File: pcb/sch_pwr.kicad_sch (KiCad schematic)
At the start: 10 parts, among them J3 Conn_01x03_Pin, U3 AP2112K-3.3, U4 AMS1117-5.0

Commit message: feat(sch): schematic review
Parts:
- removed C12, C14: 1uF, PCM_JLCPCB:C_0603, symbol PCM_JLCPCB-Capacitors:0603,1uF
- removed C15: 22uF, Capacitor_THT:CP_Radial_D4.0mm_P2.00mm, symbol EasyEDA:RVT1H220M0605
- removed H1: Jumper_Shunt, symbol Auxiliary_Items:Jumper_Shunt
- removed J3: Conn_01x03_Pin, Connector_PinHeader_2.54mm:PinHeader_1x03_P2.54mm_Vertical, symbol Connector:Conn_01x03_Pin
- removed U3: AP2112K-3.3, Package_TO_SOT_SMD:SOT-23-5, symbol Regulator_Linear:AP2112K-3.3
- removed U4: AMS1117-5.0, Package_TO_SOT_SMD:SOT-223-3_TabPin2, symbol Regulator_Linear:AMS1117-5.0
- added C14: 100uF, Capacitor_THT:CP_Radial_D5.0mm_P2.00mm, symbol PCM_JLCPCB-Capacitors:CASE-A-3216-18(mm),10uF
- added C27: 10uF, Capacitor_THT:CP_Radial_D5.0mm_P2.00mm, symbol PCM_JLCPCB-Capacitors:CASE-A-3216-18(mm),10uF
- added C28: 4.7uF, Capacitor_THT:CP_Radial_D5.0mm_P2.00mm, symbol PCM_JLCPCB-Capacitors:CASE-A-3216-18(mm),10uF
- added D3: D, Diode_SMD:D_SMA, symbol Device:D
- added D9: PLZ3V3B, Diode_SMD:D_SMF, symbol Device:D_Schottky
- added F1, F2: Polyfuse, Fuse:Fuse_1206_3216Metric, symbol Device:Polyfuse
- added SW2: SW_Lever_RSPRO_5MS1, library:SW_Lever_RSPRO_5MS1, symbol library:SW_Lever_RSPRO_5MS1
- added U2: LD1117S33TR_SOT223, Package_TO_SOT_SMD:SOT-223-3_TabPin2, symbol Regulator_Linear:LD1117S33TR_SOT223
- added U3: LD1117S50TR_SOT223, Package_TO_SOT_SMD:SOT-223-3_TabPin2, symbol Regulator_Linear:LD1117S50TR_SOT223
- C13: value 10uF -> 1uF; footprint PCM_JLCPCB:C_CASE-A-3216-18(mm) -> Capacitor_THT:CP_Radial_D5.0mm_P2.00mm; Rated Voltage 16V -> 25V
- D8: value D_Schottky -> PLZ5V1B; footprint Diode_SMD:D_SOD-323 -> Diode_SMD:D_SMF
- DC1: footprint EasyEDA:DC-IN-TH_DC-005-A200 -> Connector_BarrelJack:BarrelJack_Horizontal
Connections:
- net +3V3: now also F2.1
- net +5V: now also C27.1, SW2.2 (B), U2.3 (VI)
- net +E5V: now also F1.1, SW2.1 (A)
- net +U5V: now also SW2.3 (C)
- net GND: now also C14.2, C27.2, C28.2, D9.2 (A), U2.1 (GND), U3.1 (GND)
- net VIN: now also D3.1 (K), U3.3 (VI); no longer DC1.1
- new net: C28.1, F1.2, U3.2 (VO)
- new net: C14.1, D9.1 (K), F2.2, U2.2 (VO)
- new net: D3.2 (A), DC1.1

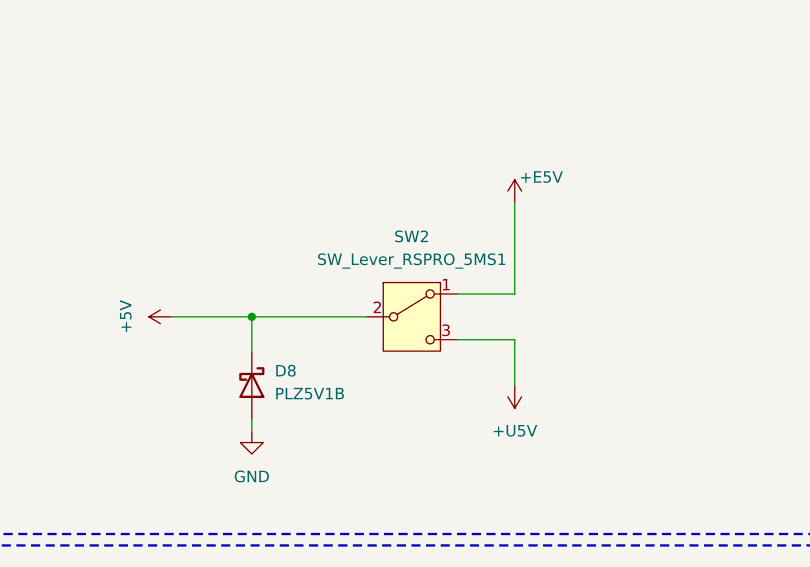
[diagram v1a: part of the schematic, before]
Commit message: feat(layout): component placement
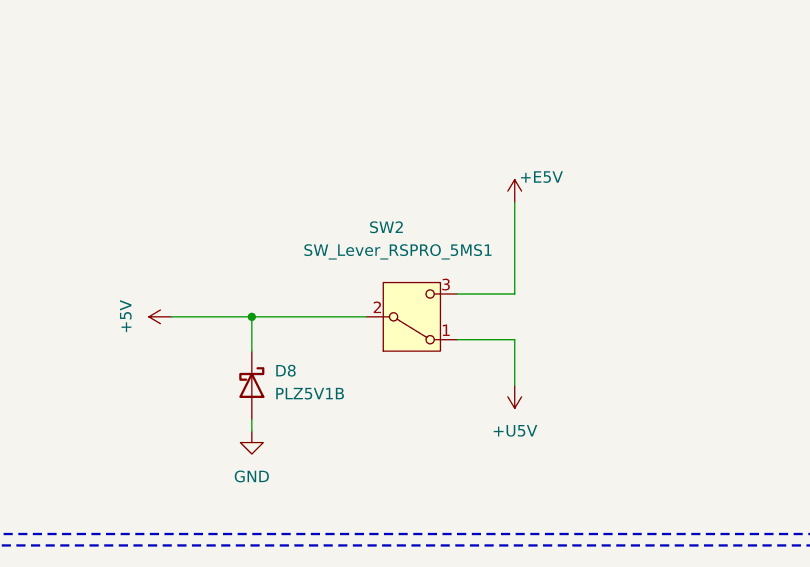
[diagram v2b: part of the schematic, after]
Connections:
- net +E5V: now also SW2.3 (C); no longer SW2.1 (A)
- net +U5V: now also SW2.1 (A); no longer SW2.3 (C)
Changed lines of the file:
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@@
+	(wire
+		(pts
+			(xy 179.07 68.58) (xy 185.42 68.58)
+		)
+		(stroke
+			(width 0)
+			(type default)
+		)
+	)
 	(wire
 		(pts
@@
 	(wire
 		(pts
-			(xy 68.58 115.57) (xy 76.2 115.57)
+			(xy 179.07 63.5) (xy 185.42 63.5)
 		)
 		(stroke
@@
 	(wire
 		(pts
-			(xy 100.33 60.96) (xy 104.14 60.96)
+			(xy 68.58 115.57) (xy 76.2 115.57)
 		)
 		(stroke
@@
 	(wire
 		(pts
-			(xy 190.5 114.3) (xy 187.96 114.3)
+			(xy 100.33 60.96) (xy 104.14 60.96)
 		)
 		(stroke
@@
 	(wire
 		(pts
-			(xy 104.14 60.96) (xy 104.14 62.23)
+			(xy 190.5 114.3) (xy 187.96 114.3)
 		)
 		(stroke
@@
 	(wire
 		(pts
-			(xy 177.8 115.57) (xy 187.96 115.57)
+			(xy 104.14 60.96) (xy 104.14 62.23)
 		)
 		(stroke
@@
 	(wire
 		(pts
-			(xy 104.14 58.42) (xy 104.14 60.96)
+			(xy 177.8 115.57) (xy 187.96 115.57)
 		)
 		(stroke
@@
 	(wire
 		(pts
-			(xy 68.58 124.46) (xy 68.58 125.73)
+			(xy 104.14 58.42) (xy 104.14 60.96)
 		)
 		(stroke
@@
 	(wire
 		(pts
-			(xy 185.42 63.5) (xy 179.07 63.5)
+			(xy 68.58 124.46) (xy 68.58 125.73)
 		)
 		(stroke
@@
 		(pts
 			(xy 168.91 66.04) (xy 156.21 66.04)
-		)
-		(stroke
-			(width 0)
-			(type default)
-		)
-	)
-	(wire
-		(pts
-			(xy 185.42 68.58) (xy 179.07 68.58)
 		)
 		(stroke
@@
 		(lib_id "library:SW_Lever_RSPRO_5MS1")
 		(at 173.99 66.04 0)
+		(mirror x)
 		(unit 1)
 		(body_style 1)
@@
 		(in_pos_files yes)
 		(dnp no)
-		(fields_autoplaced yes)
 		(property "Reference" "SW2"
-			(at 173.99 57.15 0)
+			(at 171.196 56.134 0)
 			(show_name no)
 			(do_not_autoplace no)
@@
 		)
 		(property "Value" "SW_Lever_RSPRO_5MS1"
-			(at 173.99 59.69 0)
+			(at 172.466 58.674 0)
 			(show_name no)
 			(do_not_autoplace no)
@@
 		)
 		(property "Footprint" "library:SW_Lever_RSPRO_5MS1"
-			(at 173.99 76.2 0)
+			(at 173.99 55.88 0)
 			(hide yes)
 			(show_name no)
@@
 		)
 		(property "Datasheet" ""
-			(at 173.99 73.66 0)
-			(hide yes)
-			(show_name no)
+			(at 173.99 58.42 0)
+			(hide yes)
+			(show_name no)
